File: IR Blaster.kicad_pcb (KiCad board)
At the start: 2 copper layers, 46.2 x 35.5 mm, 47 parts, among them CON1 AVR-ISP-6, IC1 ATMEGA328P-A, P1 FTDI Header, P2 IR Receiver, P3 A0-3 Inputs, P4 PWR, Q1 MMBT4401, U1 ATSHA204A, U2 NRF24L01, U3 AT25DF512C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

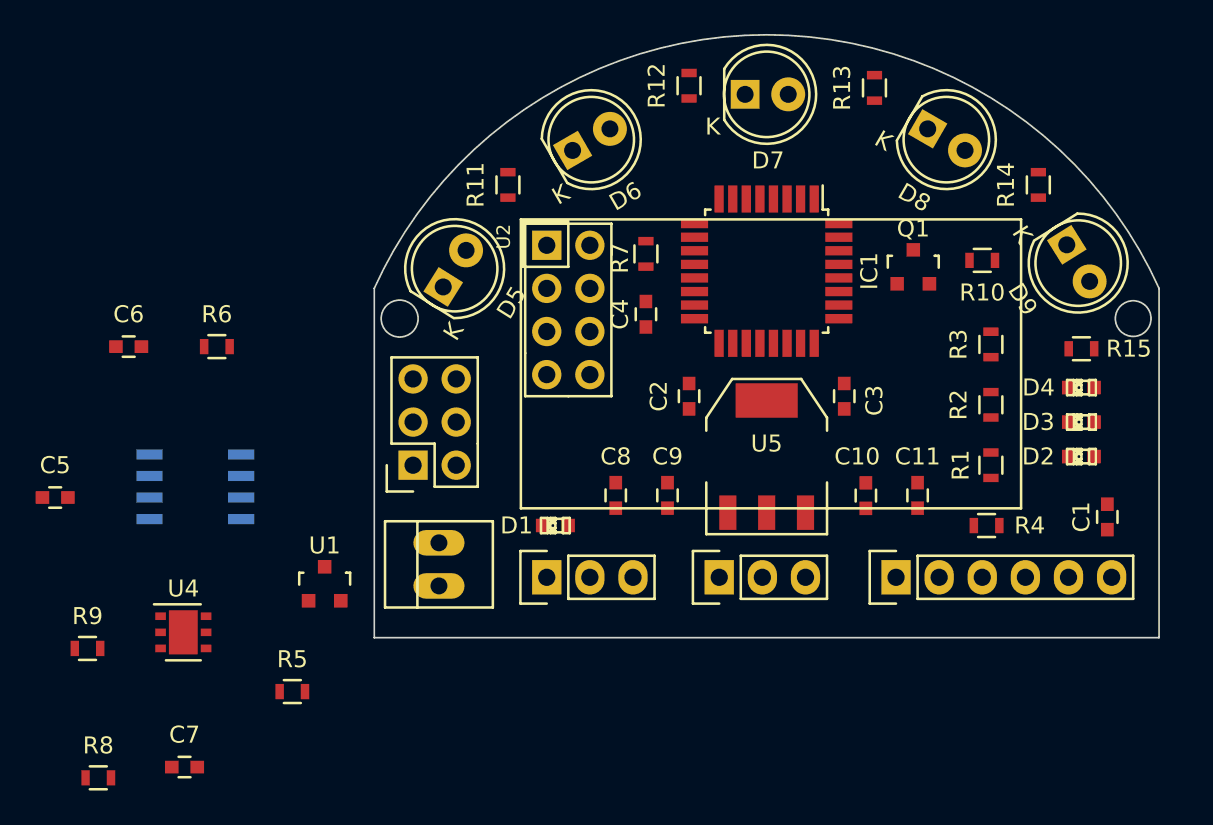
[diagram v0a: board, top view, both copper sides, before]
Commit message: Modified design to increase LEDs from 5 @30 degrees to 7 @22.5 degrees to cover 180 degrees with greater distance using narrower angluar displacement IR LEDs.  Completed electrical traces except for optional A0-A1 inputs.
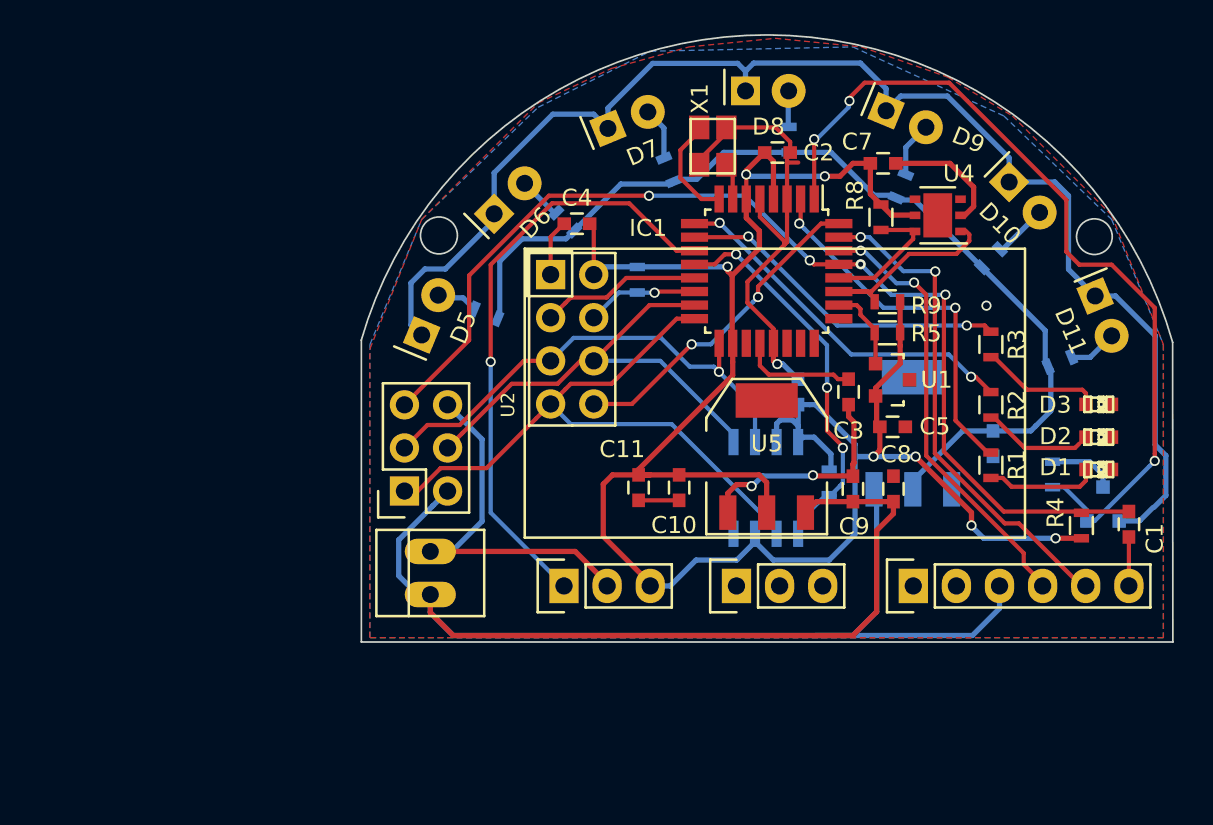
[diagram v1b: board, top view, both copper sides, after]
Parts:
- removed the D2 at (153.2, 103.6)
- added C12: 22uF, Capacitors_SMD:C_0603, B.Cu at (148.0, 102.9)
- added D10: IR LED, MySensors-BBL:LED-5MM-Horizontal, F.Cu at (148.9, 87.5)
- added D11: IR LED, MySensors-BBL:LED-5MM-Horizontal, F.Cu at (154.0, 94.2)
- added R16: R, Resistors_SMD:R_0603, B.Cu at (147.8, 91.9)
- added R17: R, Resistors_SMD:R_0603, B.Cu at (151.9, 98.0)
- added U6: AMS1117-5.0, SMD_Packages:SOT-223, B.Cu at (143.2, 102.3)
- added X1: CRYSTAL, Crystals_Oscillators_SMD:crystal_FA238-TSX3225, F.Cu at (131.4, 85.3)
- C6, R11, R12, R13, R14, R15, R6, R7: moved to B.Cu
- D1: value Led_Small -> Err
- D5, D6, D7, D8, D9: footprint LEDs:LED-5MM -> MySensors-BBL:LED-5MM-Horizontal
- P3: value A0-3 Inputs -> Analog IN
- Q1: value MMBT4401 -> FDV303N; moved to B.Cu
- R10: value 67.5 -> 10k; moved to B.Cu
- moved R8 56.7 mm to (141.4, 89.5), turned to 90 degrees
- moved C7 54.4 mm to (141.5, 86.4)
- moved R9 51.4 mm to (141.7, 94.5), turned to 180 degrees
- moved U4 50.8 mm to (144.7, 89.4), turned to 180 degrees
- moved C5 49.5 mm to (142.0, 101.9)
- moved R5 40.9 mm to (141.7, 96.3), turned to 180 degrees
- moved C6 39.5 mm to (136.5, 99.8), turned to 90 degrees
- moved R6 36.9 mm to (138.3, 105.2), turned to 270 degrees
- moved U1 35.5 mm to (142.0, 99.1), turned to 270 degrees
- moved U3 33.6 mm to (134.6, 105.5), turned to 90 degrees
- moved D1 32.2 mm to (154.2, 104.4), turned to 180 degrees
- moved Q1 17.9 mm to (154.4, 106.4), turned to 180 degrees
- moved C11 16.4 mm to (127.1, 105.5), turned to 270 degrees
- moved C8 16.4 mm to (142.1, 105.5)
- moved C2 15.3 mm to (135.3, 85.7), turned to 0 degrees
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- renumbered D3 to D2, D4 to D3
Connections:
- D1 pad 2: /SCK -> Net-(D1-Pad2)
- D5 pad 1: Net-(D5-Pad1) -> Net-(D10-Pad1)
- D6 pad 1: Net-(D5-Pad1) -> Net-(D10-Pad1)
- D7 pad 1: Net-(D5-Pad1) -> Net-(D10-Pad1)
- D8 pad 1: Net-(D5-Pad1) -> Net-(D10-Pad1)
- D9 pad 1: Net-(D5-Pad1) -> Net-(D10-Pad1)
- IC1 pad 7: Net-(IC1-Pad7) -> /XTAL1
- IC1 pad 8: Net-(IC1-Pad8) -> /XTAL2
- Q1 pad 1: GND -> Net-(D10-Pad1)
- Q1 pad 2: Net-(Q1-Pad2) -> /D3
- Q1 pad 3: Net-(D5-Pad1) -> GND
- R1 pad 1: Net-(D2-Pad2) (its old number) -> Net-(D1-Pad2)
- R10 pad 1: Net-(Q1-Pad2) -> GND
- R11 pad 1: +3V3 -> +5V
- R12 pad 1: +3V3 -> +5V
- R13 pad 1: +3V3 -> +5V
- R14 pad 1: +3V3 -> +5V
- R15 pad 1: +3V3 -> +5V
- R8 pad 1: +3V3 -> /SCL
- R8 pad 2: /SCL -> +3V3
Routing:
- net +3V3: track 0.00 -> 132.6 mm, vias 0 -> 7
- net VCC: track 0.00 -> 97.9 mm
- net Net-(D10-Pad1): track 0.00 -> 81.8 mm
- net GND: track 0.00 -> 81.5 mm, vias 0 -> 3
- net /RESET: track 0.00 -> 63.3 mm, vias 0 -> 4
- net +5V: track 0.00 -> 57.6 mm
- net /D3: track 0.00 -> 50.2 mm, vias 0 -> 3
- net /MISO: track 0.00 -> 38.5 mm
- net /D7: track 0.00 -> 35.4 mm, vias 0 -> 1
- net /SCK: track 0.00 -> 29.3 mm, vias 0 -> 1
- net /TXD: track 0.00 -> 29.2 mm, vias 0 -> 2
- net /MOSI: track 0.00 -> 28.6 mm
- net /RXD: track 0.00 -> 26.2 mm, vias 0 -> 2
- net /D8: track 0.00 -> 24.1 mm, vias 0 -> 3
- net /D4: track 0.00 -> 22.1 mm, vias 0 -> 2
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- added copper zone on B.Cu, net GND
- added copper zone on F.Cu, net GND
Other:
- board size 46.2 x 35.5 mm -> 47.8 x 35.8 mm
- net class 1A added: clearance 0.2, trace_width 0.31, via_dia 0.6, via_drill 0.4

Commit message: General PCB tidying.  Added board identifier and OSHW logo, tweaked LED orientation, corrected paths for 3d model view, added top-side silk screen identifiers for connectors, re-oriented ISCP connector, etc.
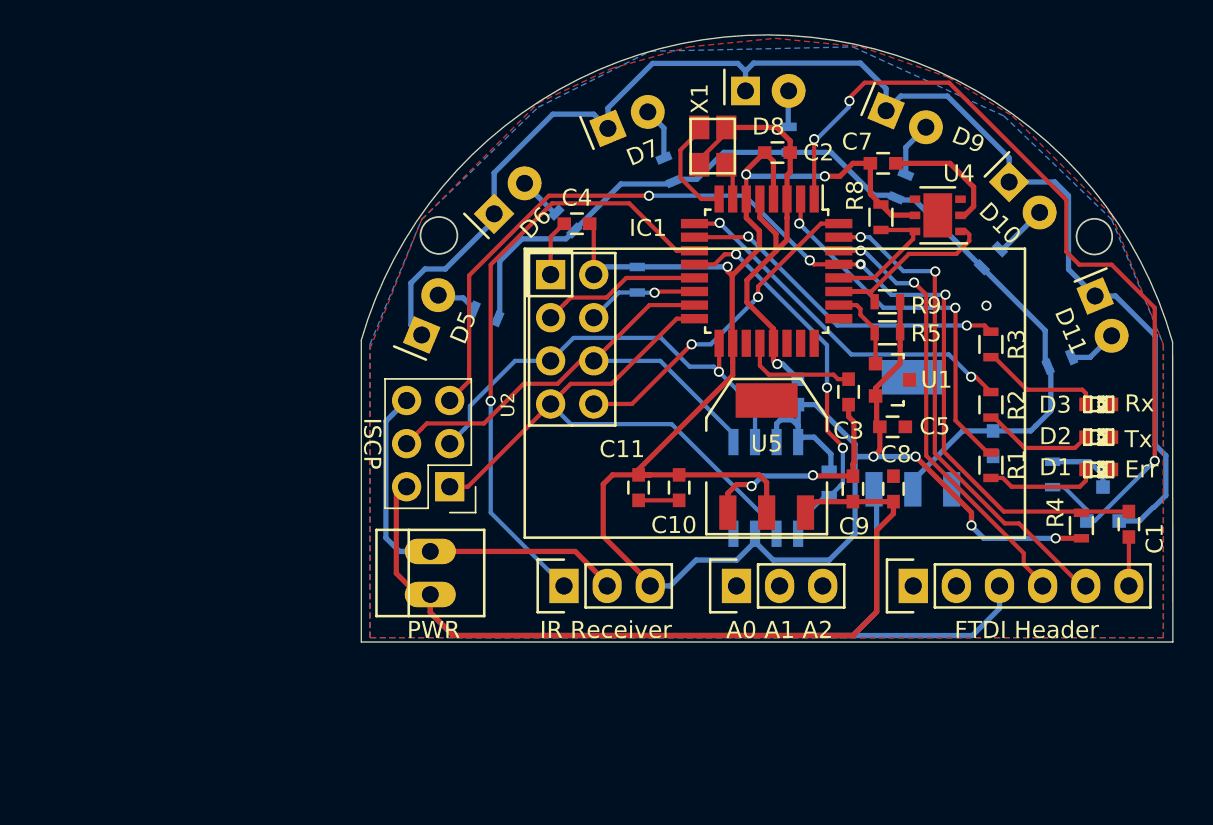
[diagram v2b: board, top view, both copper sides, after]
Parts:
- added G***: LOGO, LOGO, B.Cu at (125.6, 107.7)
- CON1: moved to B.Cu
- moved CON1 2.68 mm to (116.0, 105.4)
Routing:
- net /MISO: track 38.5 -> 35.7 mm
- net /MOSI: track 28.6 -> 30.9 mm
- net /SCK: track 29.3 -> 27.1 mm
- net /RESET: track 63.3 -> 61.9 mm
- net VCC: track 97.9 -> 99.3 mm
- net GND: track 81.5 -> 82.6 mm
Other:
- board text added: "A0 A1 A2"
- board text added: "Err"
- board text added: "FTDI Header"
- board text added: "IR Receiver"
- board text added: "ISCP"
- board text added: "MySensors.org IR Blaster Version 0.4"
- board text added: "PWR"
- board text added: "Rx"
- board text added: "Tx"

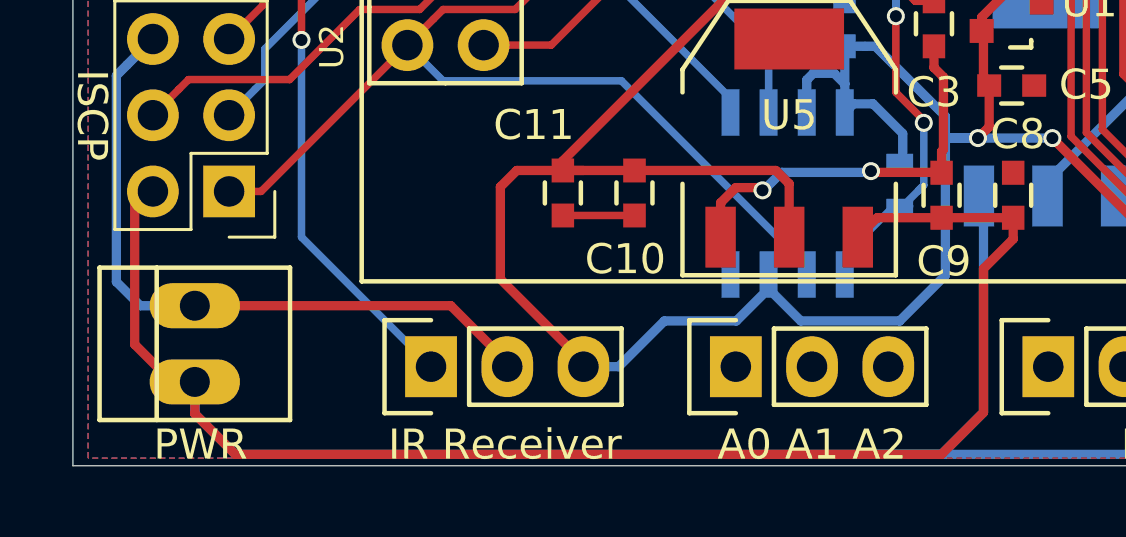
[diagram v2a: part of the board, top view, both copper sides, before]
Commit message: Cleaned up 3D parts (power terminal block and 0603 LEDs) in preparation for v0.4 post and review.
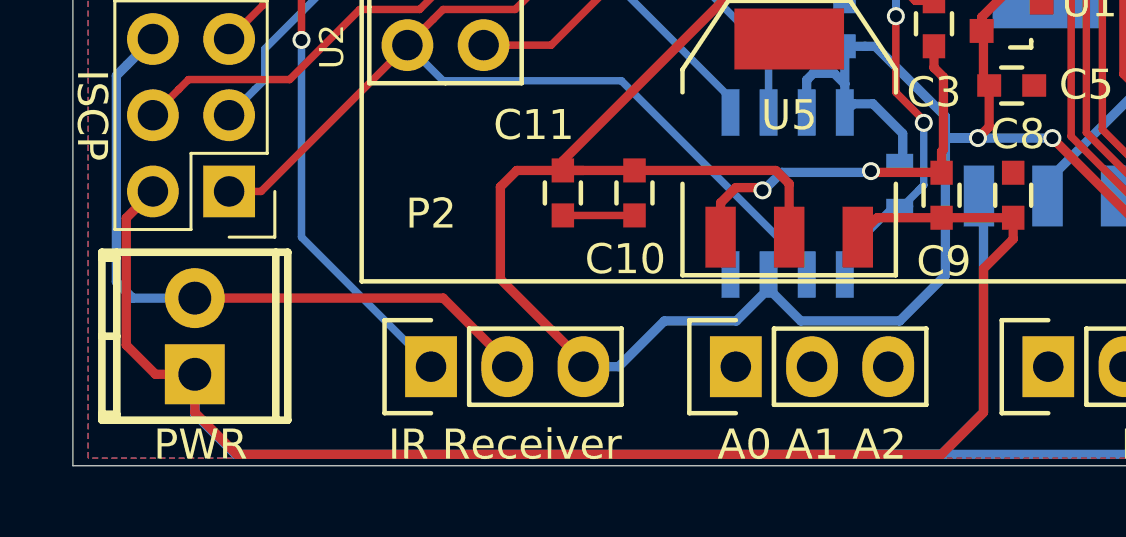
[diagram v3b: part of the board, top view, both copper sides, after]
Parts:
- P2: footprint Pin_Headers:Pin_Header_Straight_1x03 -> Socket_Strips:Socket_Strip_Straight_1x03
- P4: footprint Connect:PINHEAD1-2 -> TerminalBlock2.54mmx2
- moved P4 0.25 mm to (114.8, 110.2), turned to 270 degrees
- turned P2 to 0 degrees
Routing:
- net GND: track 82.6 -> 81.6 mm
- net VCC: track 99.3 -> 100.0 mm

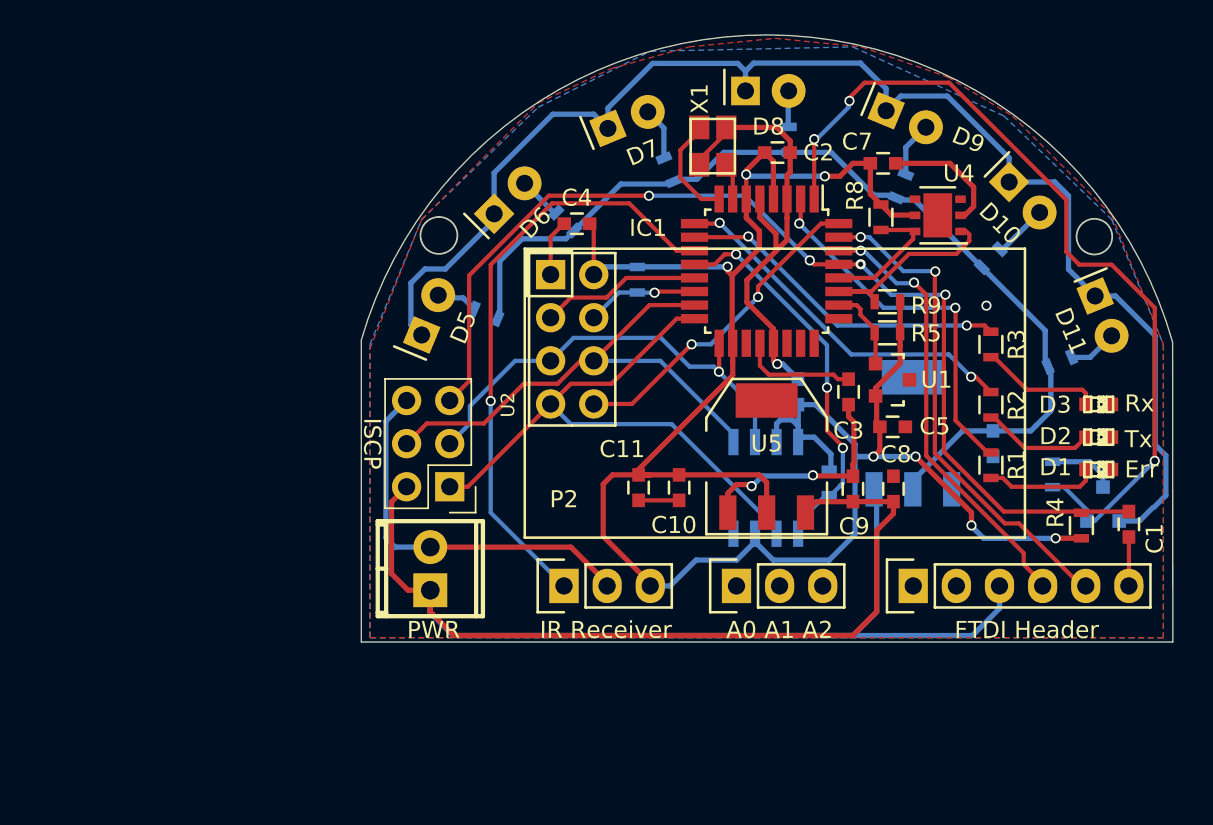
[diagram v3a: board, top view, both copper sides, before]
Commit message: Project should now be location independent users who have established mysensors part management prequisites as defined on https://github.com/mysensors-kicad/part_management.  Implemented MySensors path conventions and moved all needed parts from personal bblacey library to appropriate mysensors symbol, footprint or 3dparts github repos and modified the corresponding schematic, pcb and associated net and cmp references accordingly.
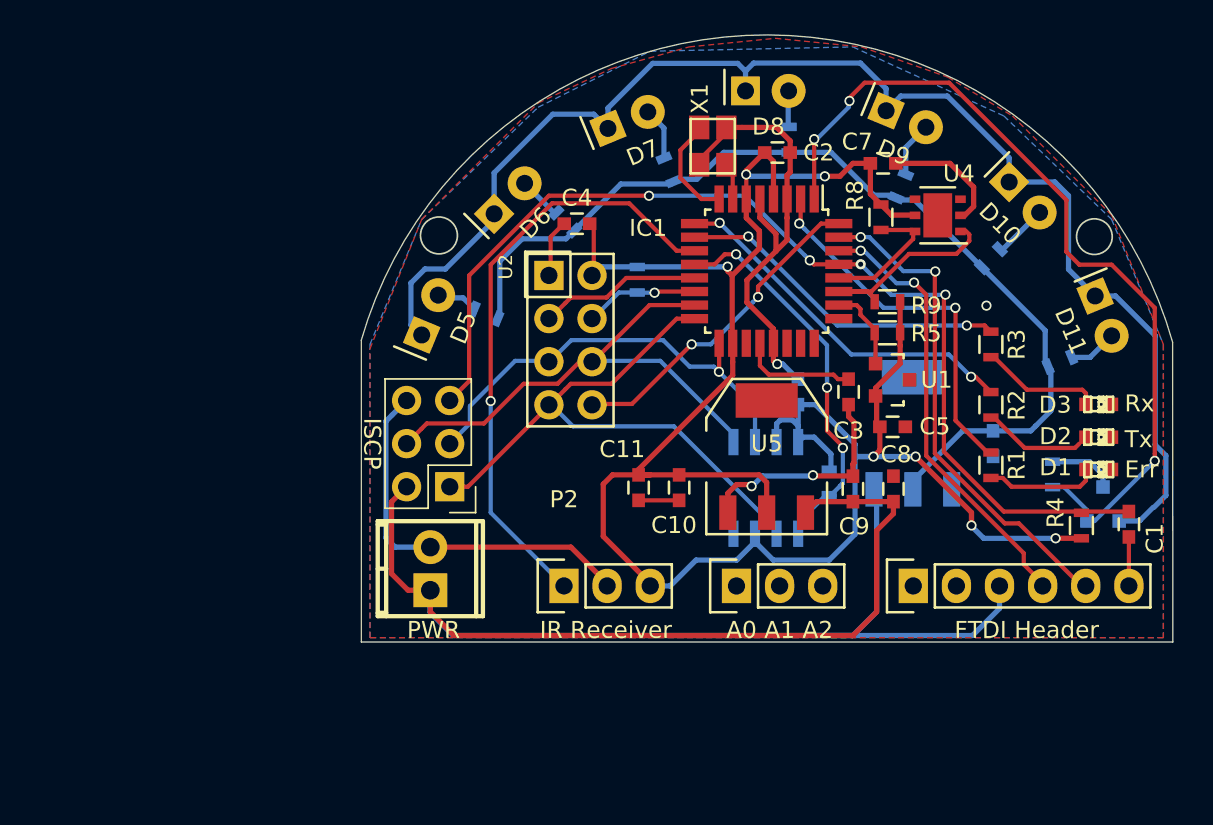
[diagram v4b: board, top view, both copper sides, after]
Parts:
- D10, D11, D5, D6, D7, D8, D9: footprint MySensors-BBL:LED-5MM-Horizontal -> mysensors_leds:LED-5MM-Horizontal
- P4: footprint TerminalBlock2.54mmx2 -> mysensors_connectors:TerminalBlock2.54mmx2-kcswalter
- U2: footprint MySensors_Radios:NRF24L01 -> mysensors_radios:NRF24L01
- moved U2 9.24 mm to (120.3, 91.4)
